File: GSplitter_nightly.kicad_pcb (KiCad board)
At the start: 2 copper layers, 81.5 x 44.4 mm, 23 parts, among them J1 DC_JACK, T1 SCREW, T2 SCREW, U1 LM7805, U2 ICL7660

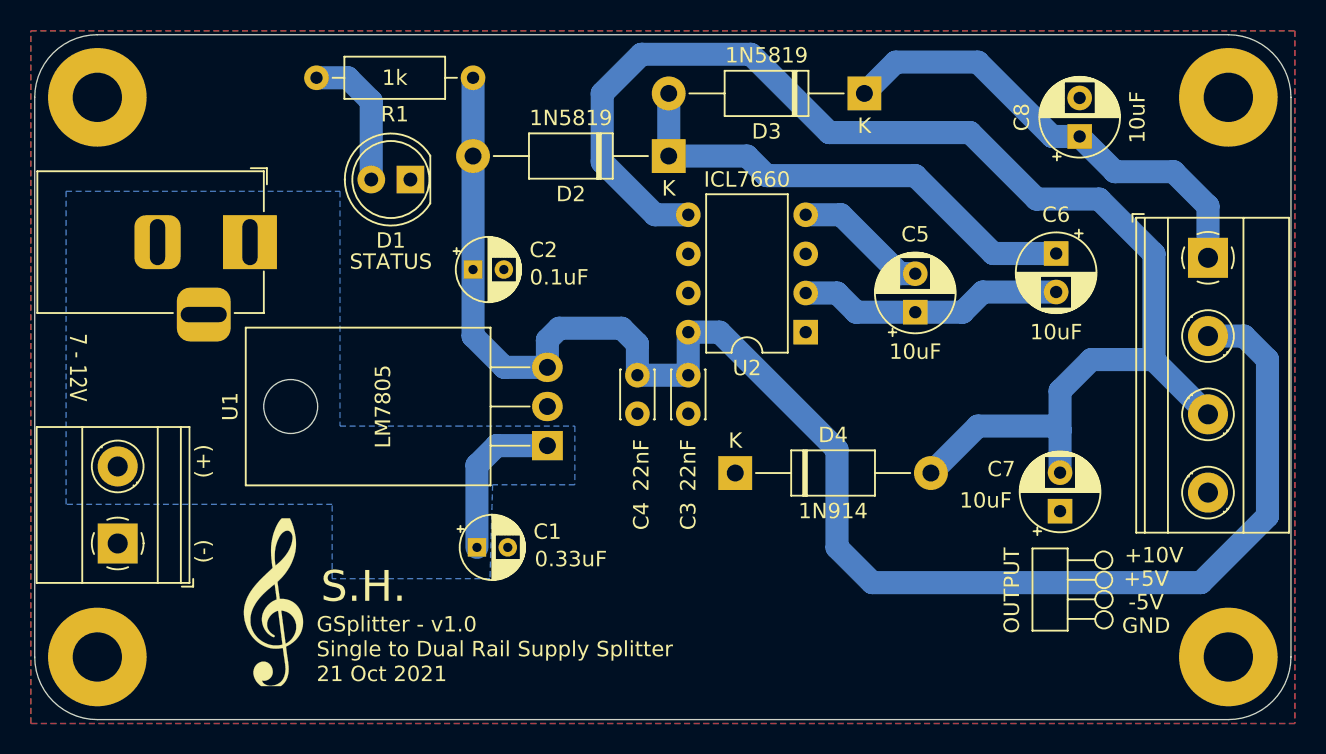
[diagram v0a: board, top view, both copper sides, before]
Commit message: Smooth out the VSUPPLY net fill zone
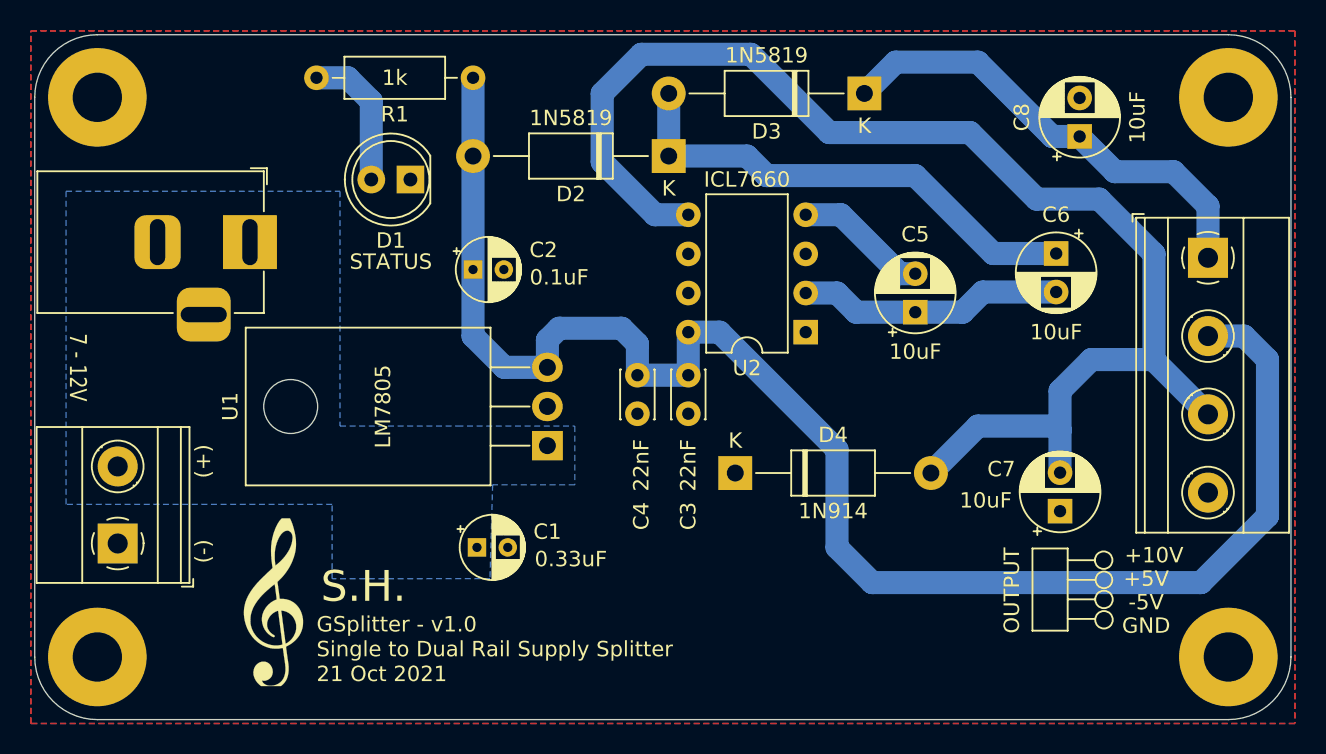
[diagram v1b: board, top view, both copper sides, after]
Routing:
- net VSUPPLY: track 10.4 -> 0.00 mm
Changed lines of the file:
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@@
     (style (thickness 0.15) (arrow_length 1.27) (text_position_mode 2) (extension_height 0.58642) (extension_offset 0))
   )
-  (segment (start 53.594 65.278) (end 54.864 64.008) (width 1.5) (layer "B.Cu") (net 1))
-  (segment (start 53.594 70.612) (end 53.594 65.278) (width 1.5) (layer "B.Cu") (net 1))
-  (segment (start 54.864 64.008) (end 58.166 64.008) (width 1.5) (layer "B.Cu") (net 1))
   (segment (start 64.008 57.404) (end 64.008 59.436) (width 1.5) (layer "B.Cu") (net 3))
   (segment (start 58.166 57.15) (end 58.928 56.388) (width 1.5) (layer "B.Cu") (net 3))
@@
     )
   )
-  (zone (net 2) (net_name "GND") (layer "B.Cu") (hatch edge 0.508)
+  (zone (net 2) (net_name "GND") (layers F&B.Cu) (hatch edge 0.508)
     (connect_pads (clearance 0.5))
     (min_thickness 0.254) (filled_areas_thickness no)
@@
     (connect_pads (clearance 0.5))
     (min_thickness 0.254) (filled_areas_thickness no)
-    (fill yes (thermal_gap 0.508) (thermal_bridge_width 1.3))
+    (fill yes (thermal_gap 0.508) (thermal_bridge_width 1.3) (smoothing fillet) (radius 2))
     (polygon
       (pts
